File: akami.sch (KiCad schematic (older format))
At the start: 64 parts, among them J1 USB_C_Receptacle_USB2.0, J2 Conn_01x01, J3 Conn_01x01, Q2 AO3401A, U1 nRF52840, U2 TP4054, U3 LP5912-3.3DRV, U4 ProMicro_2, Y1 32MHz, Y2 32.768 kHz

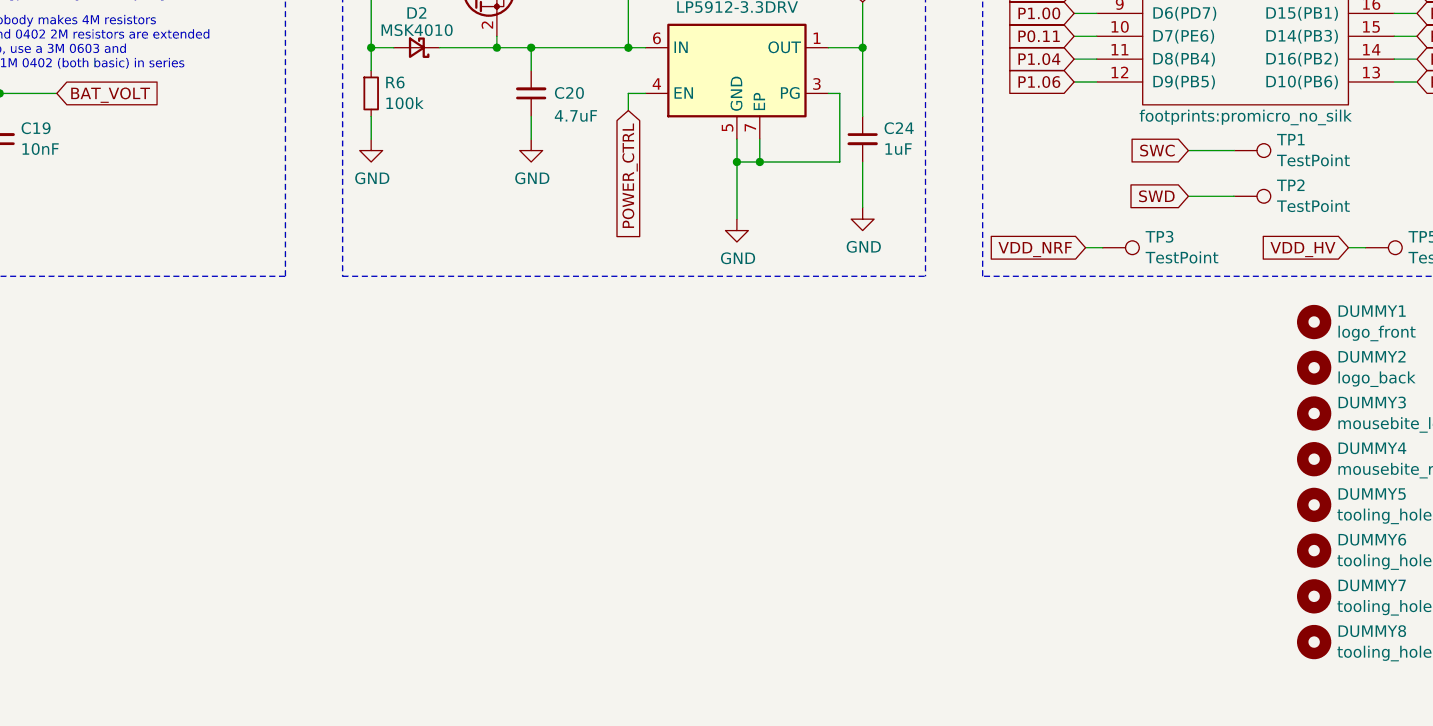
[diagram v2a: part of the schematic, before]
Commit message: rev 3A (lv): preliminary circuit
it's basically the original low-voltage circuit, but with another
mosfet to control the second EXT pin, with a schottky in parallel
to reduce Vf across the mosfet.

it should work, but it's sad that it has to be low voltage. it also
requires an additional extended part for a smaller footprint mosfet
because no way can we fit 3 SOT-23s on the board currently.
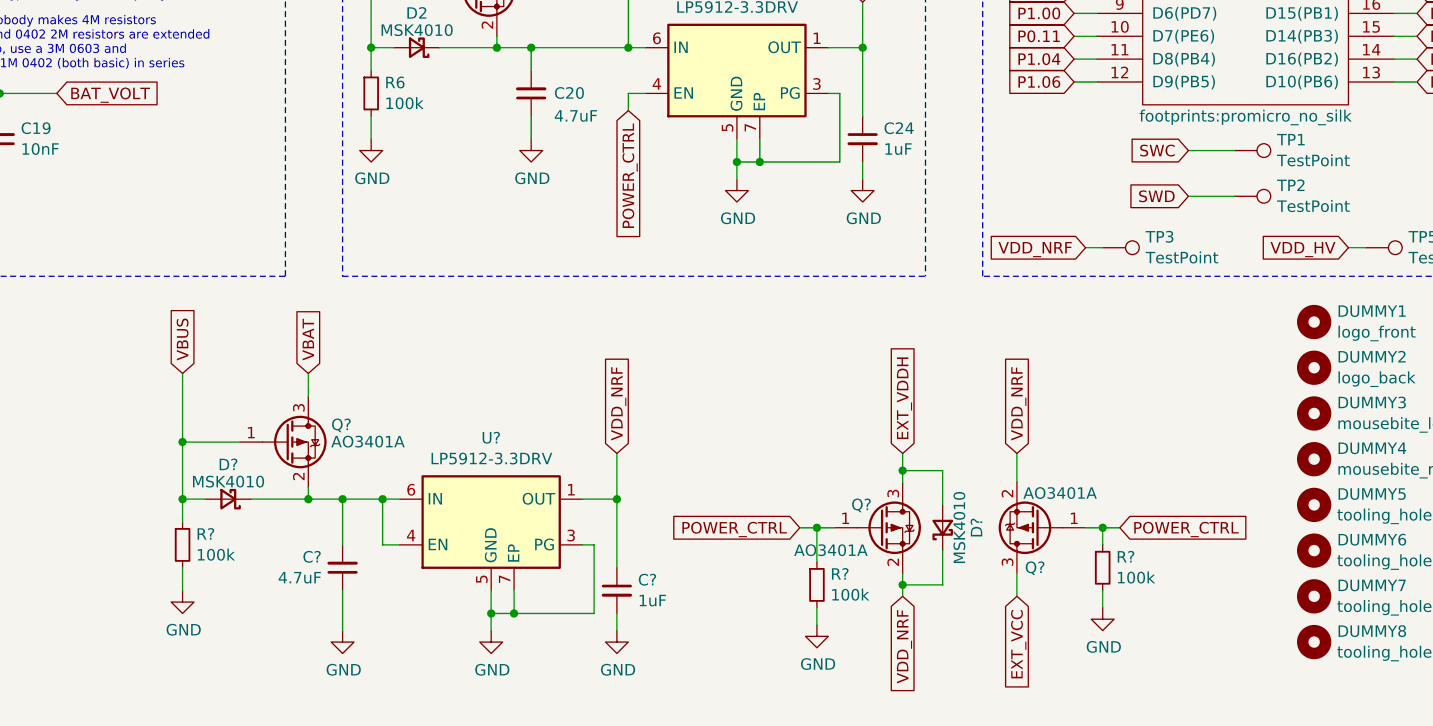
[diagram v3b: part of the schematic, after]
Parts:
- added C?: 1uF, Capacitor_SMD:C_0402_1005Metric, symbol Device:C_Small
- added C?: 4.7uF, Capacitor_SMD:C_0603_1608Metric, symbol Device:C_Small
- added D? (x2): MSK4010, Diode_SMD:D_SOD-523, symbol Device:D_Schottky_Small
- added Q? (x3): AO3401A, Package_TO_SOT_SMD:SOT-23, symbol Transistor_FET:IRLML9301
- added R? (x3): 100k, Resistor_SMD:R_0402_1005Metric, symbol Device:R_Small
- added U?: LP5912-3.3DRV, Package_SON:WSON-6-1EP_2x2mm_P0.65mm_EP1x1.6mm_ThermalVias, symbol Regulator_Linear:LP5912-3.3DRV
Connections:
- net EXT_VCC: now also Q?.3 (D)
- net GND: now also C?.1, C?.2, R?.2, R?.2, R?.2, U?.3 (PG), U?.5 (GND), U?.7 (EP)
- net POWER_CTRL: now also Q?.1 (G), Q?.1 (G), R?.1, R?.1
- net VBAT: now also Q?.3 (D)
- net VBUS: now also D?.2 (A), Q?.1 (G), R?.1
- net VDD_NRF: now also C?.1, D?.1 (K), Q?.2 (S), Q?.2 (S), U?.1 (OUT)
- new net: C?.2, D?.1 (K), Q?.2 (S), U?.4 (EN), U?.6 (IN)
- new net EXT_VDDH: D?.2 (A), Q?.3 (D)

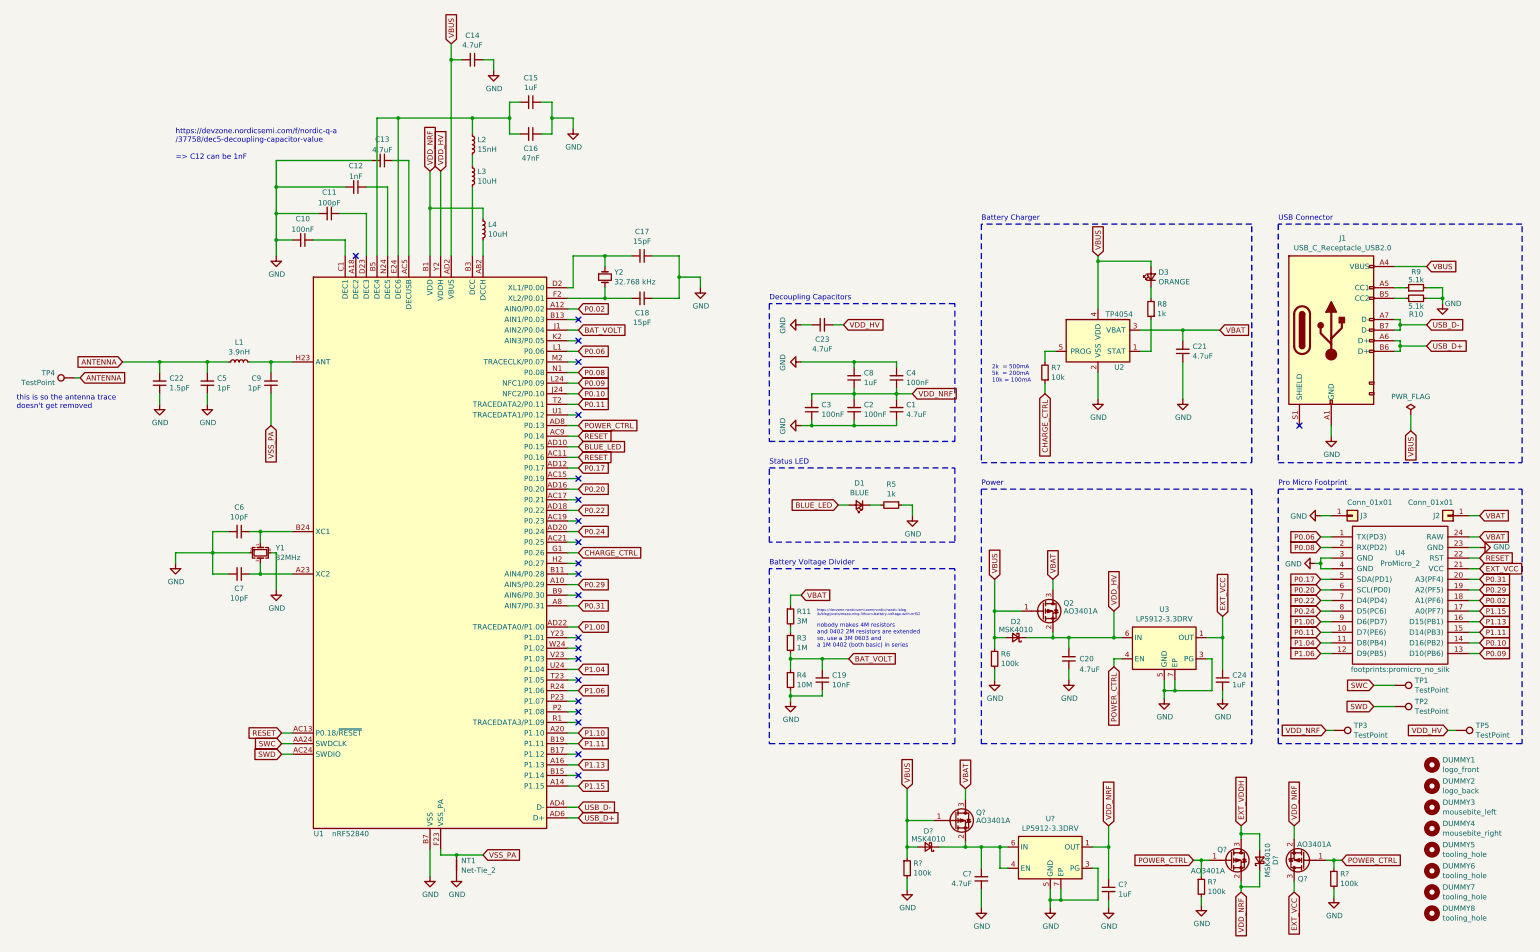
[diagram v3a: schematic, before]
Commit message: continue placement and routing on 3A
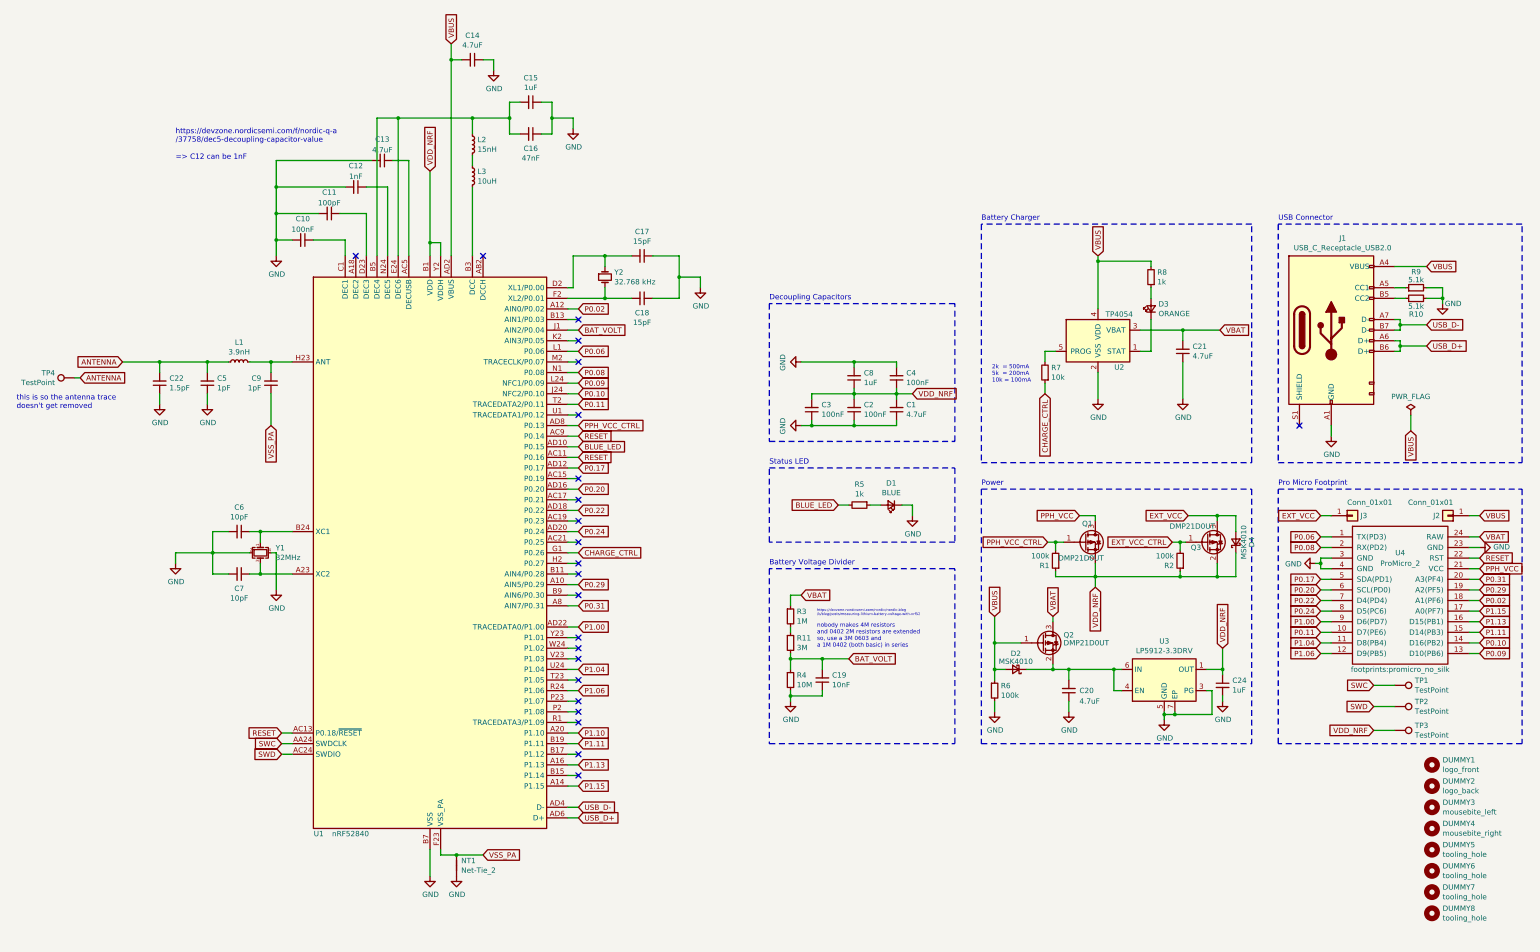
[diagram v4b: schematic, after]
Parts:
- removed C23, C?: 4.7uF, Capacitor_SMD:C_0603_1608Metric, symbol Device:C_Small
- removed C?: 1uF, Capacitor_SMD:C_0402_1005Metric, symbol Device:C_Small
- removed D? (x2): MSK4010, Diode_SMD:D_SOD-523, symbol Device:D_Schottky_Small
- removed L4: 10uH, Inductor_SMD:L_0603_1608Metric, symbol Device:L_Small
- removed Q? (x2): AO3401A, Package_TO_SOT_SMD:SOT-23, symbol Transistor_FET:IRLML9301
- removed R? (x2): 100k, Resistor_SMD:R_0402_1005Metric, symbol Device:R_Small
- removed TP5: TestPoint, TestPoint:TestPoint_Pad_1.0x1.0mm, symbol Connector:TestPoint
- removed U?: LP5912-3.3DRV, Package_SON:WSON-6-1EP_2x2mm_P0.65mm_EP1x1.6mm_ThermalVias, symbol Regulator_Linear:LP5912-3.3DRV
- added D4: MSK4010, Diode_SMD:D_SOD-523, symbol Device:D_Schottky_Small
- added Q3: DMP21D0UT, Package_TO_SOT_SMD:SOT-523, symbol Transistor_FET:IRLML9301
- added R2: 100k, Resistor_SMD:R_0402_1005Metric, symbol Device:R_Small
- Q1: renamed from Q?; value AO3401A -> DMP21D0UT; footprint Package_TO_SOT_SMD:SOT-23 -> Package_TO_SOT_SMD:SOT-523; LCSC Part C15127 -> C150733
- Q2: value AO3401A -> DMP21D0UT; footprint Package_TO_SOT_SMD:SOT-23 -> Package_TO_SOT_SMD:SOT-523; LCSC Part C15127 -> C150733
- gave numbers to parts that had none: 1
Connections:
- net BAT_VOLT: now also R11.2; no longer R3.2
- net BLUE_LED: now also R5.2; no longer D1.2 (A)
- net EXT_VCC: now also J3.1 (Pin_1), D4.2 (A), Q3.3 (D); no longer C24.1, Q1.3 (D), U3.1 (OUT), U4.21 (VCC)
- net GND: now also D1.1 (K); no longer J3.1 (Pin_1), R1.2, R5.1
- net VBAT: now also R3.1; no longer J2.1 (Pin_1), R11.1
- net VBUS: now also J2.1 (Pin_1), R8.2; no longer D3.2 (A)
- net VDD_NRF: now also C24.1, R1.1, U1.Y2 (VDDH), U3.1 (OUT), D4.1 (K), Q3.2 (S), R2.1
- net at U2.1 (STAT): now also D3.1 (K); no longer R8.1
- net POWER_CTRL renamed PPH_VCC_CTRL
- net PPH_VCC_CTRL: now also R1.2; no longer R1.1, U3.4 (EN)
- net VDD_HV: no longer names the net of C20.2, D2.1 (K), Q2.2 (S), U3.6 (IN)
- net VDD_HV: now also U3.4 (EN); no longer U1.Y2 (VDDH)
- new net: D3.2 (A), R8.1
- new net: R11.1, R3.2
- new net: D1.2 (A), R5.1
- new net EXT_VCC_CTRL: Q3.1 (G), R2.2
- new net PPH_VCC: Q1.3 (D), U4.21 (VCC)
- no-connect marks 22 -> 23
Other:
- moved on the sheet: C20, C24, D1, D2, D3, Q1, Q2, R1, R11, R3, R5, R6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

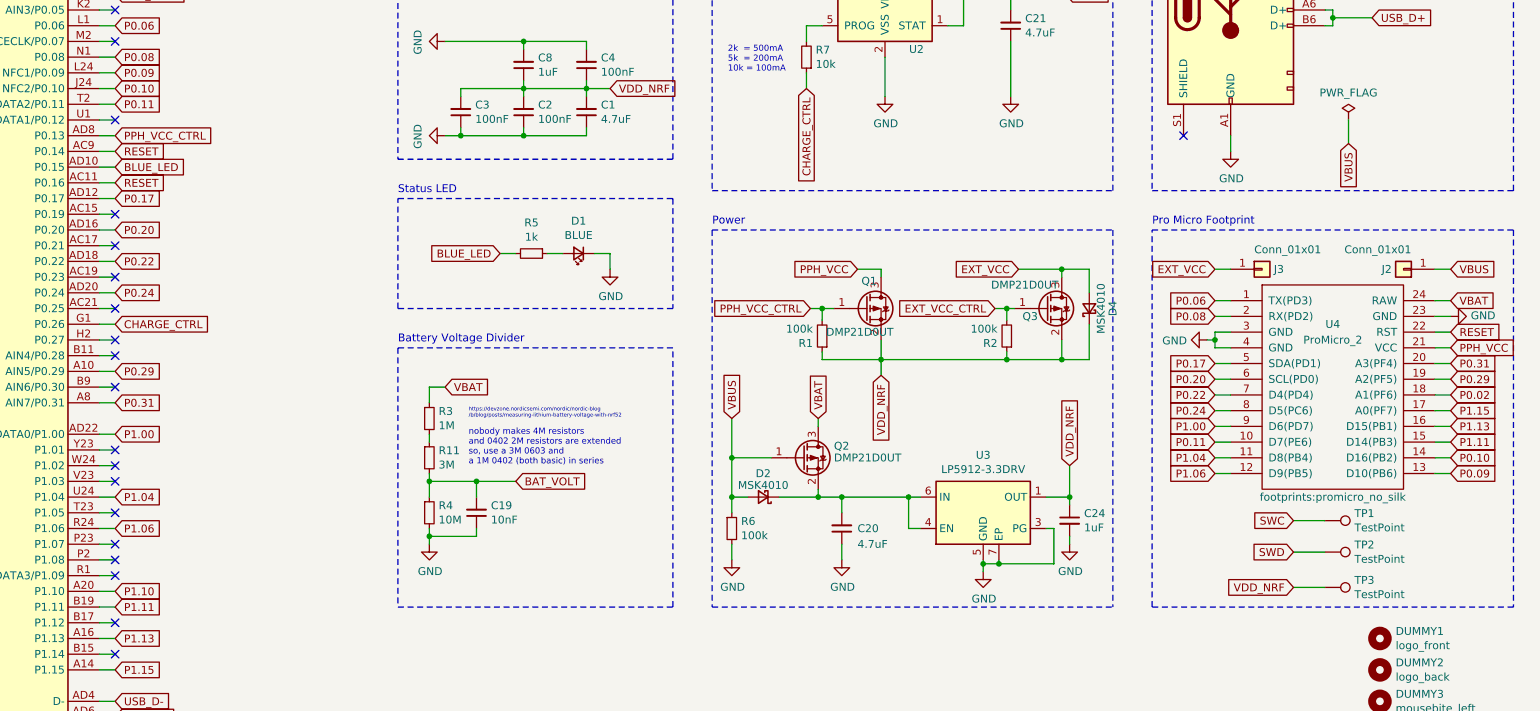
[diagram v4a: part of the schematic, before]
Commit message: rev 3 (lv): 1. layout and route all components
2. replace mosfet pullups with 1M resistors

3. silkscreen pin labelling now shows nRF52 pin numbers instead
   of promicro pins (those are "standard" and hence useless to
   print)

4. VBUS and EXT_VCC is now broken out; VBUS is coincidentally in
   the same place as an Elite-C (above RAW -- now BAT)

gerbers, BOM, and PnP files *are* updated.
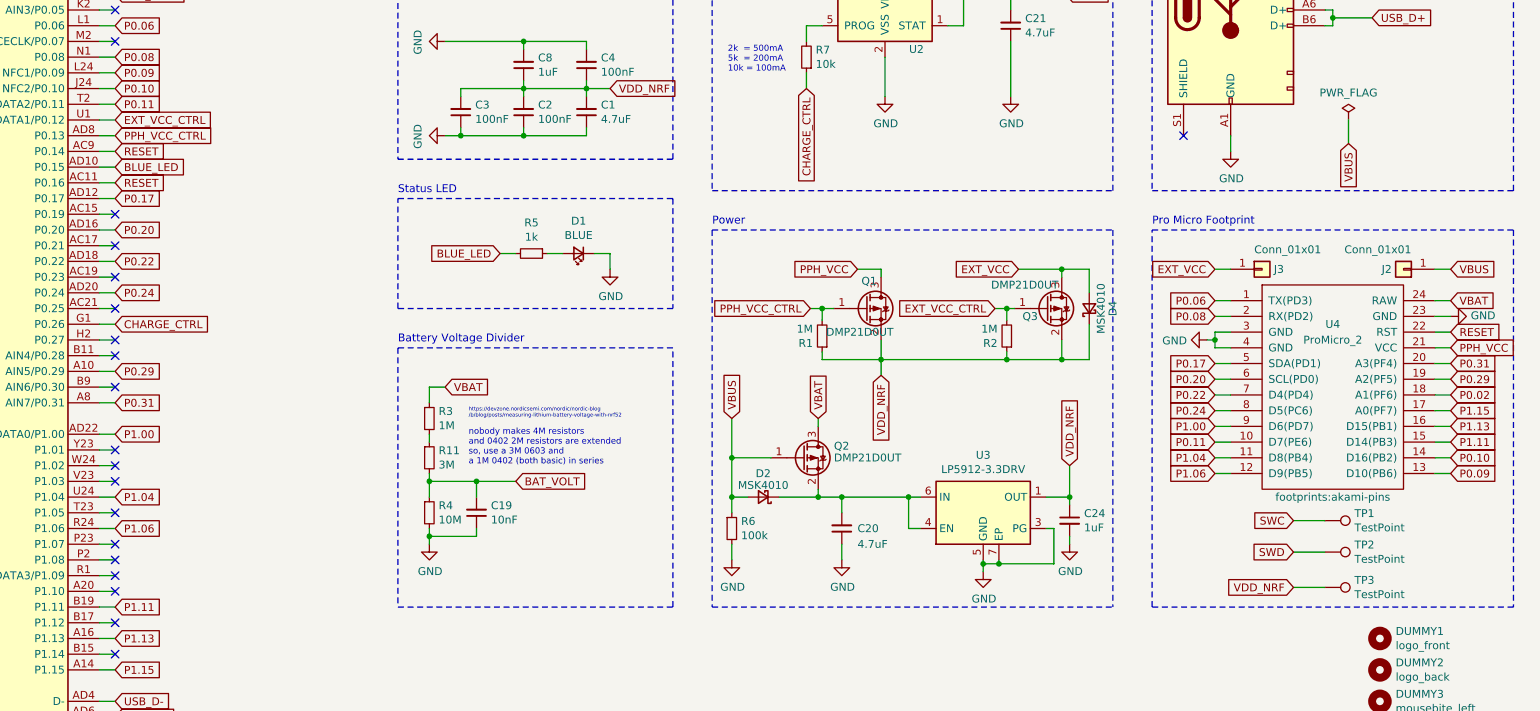
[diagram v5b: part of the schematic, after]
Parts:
- R1, R2: value 100k -> 1M; LCSC Part C25741 -> C26083
- U4: footprint footprints:promicro_no_silk -> footprints:akami-pins
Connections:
- net EXT_VCC_CTRL: now also U1.U1 (TRACEDATA1/P0.12)
- net P1.10: no longer names the net of U1.A20 (P1.10)
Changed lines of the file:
@@
 NoConn ~ 6600 3950
 NoConn ~ 6600 4150
-NoConn ~ 6600 4650
 NoConn ~ 6600 3750
 Wire Wire Line
@@
 Wire Wire Line
 	6600 4550 6500 4550
-Wire Wire Line
-	6600 4650 6500 4650
 Wire Wire Line
 	6600 5250 6500 5250
@@
 F 0 "U4" H 14350 6750 50  0000 C CNN
 F 1 "ProMicro_2" H 14350 6650 50  0000 C CNN
-F 2 "footprints:promicro_no_silk" H 14350 5650 50  0000 C CNN
+F 2 "footprints:akami-pins" H 14350 5650 50  0000 C CNN
 F 3 "" H 14300 6450 50  0001 C CNN
 	1    14350 6350
@@
 	1    0    0    -1
 $EndComp
-Text GLabel 6600 7650 2    50   Input ~ 0
-P1.10
 Wire Wire Line
 	6500 4450 6600 4450
@@
 Text GLabel 10525 6550 1    50   Input ~ 0
 VBUS
-$Comp
-L Device:R_Small R6
-U 1 1 60073401
-P 10525 7250
-F 0 "R6" H 10584 7296 50  0000 L CNN
-F 1 "100k" H 10584 7205 50  0000 L CNN
-F 2 "Resistor_SMD:R_0402_1005Metric" H 10525 7250 50  0001 C CNN
-F 3 "~" H 10525 7250 50  0001 C CNN
-F 4 "C25741" H 10525 7250 50  0001 C CNN "LCSC Part"
-	1    10525 7250
-	1    0    0    -1
-$EndComp
 Wire Wire Line
 	10525 7350 10525 7450
@@
 P 11100 6025
 F 0 "R1" H 11159 6071 50  0000 L CNN
-F 1 "100k" H 11159 5980 50  0000 L CNN
+F 1 "1M" H 11159 5980 50  0000 L CNN
 F 2 "Resistor_SMD:R_0402_1005Metric" H 11100 6025 50  0001 C CNN
 F 3 "~" H 11100 6025 50  0001 C CNN
-F 4 "C25741" H 11100 6025 50  0001 C CNN "LCSC Part"
+F 4 "C26083" H 11100 6025 50  0001 C CNN "LCSC Part"
 	1    11100 6025
 	-1   0    0    1
@@
 P 12275 6025
 F 0 "R2" H 12334 6071 50  0000 L CNN
-F 1 "100k" H 12334 5980 50  0000 L CNN
+F 1 "1M" H 12334 5980 50  0000 L CNN
 F 2 "Resistor_SMD:R_0402_1005Metric" H 12275 6025 50  0001 C CNN
 F 3 "~" H 12275 6025 50  0001 C CNN
-F 4 "C25741" H 12275 6025 50  0001 C CNN "LCSC Part"
+F 4 "C26083" H 12275 6025 50  0001 C CNN "LCSC Part"
 	1    12275 6025
 	-1   0    0    1
@@
 Wire Wire Line
 	14100 7625 14300 7625
+Wire Wire Line
+	6600 4650 6500 4650
+Text GLabel 6600 4650 2    50   Input ~ 0
+EXT_VCC_CTRL
+NoConn ~ 6600 7650
+$Comp
+L Device:R_Small R6
+U 1 1 60073401
+P 10525 7250
+F 0 "R6" H 10584 7296 50  0000 L CNN
+F 1 "100k" H 10584 7205 50  0000 L CNN
+F 2 "Resistor_SMD:R_0402_1005Metric" H 10525 7250 50  0001 C CNN
+F 3 "~" H 10525 7250 50  0001 C CNN
+F 4 "C25741" H 10525 7250 50  0001 C CNN "LCSC Part"
+	1    10525 7250
+	1    0    0    -1
+$EndComp
 $EndSCHEMATC
